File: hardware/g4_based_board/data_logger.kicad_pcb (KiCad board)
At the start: 4 copper layers, 100 x 100 mm, 115 parts, among them J1 Conn_01x07_Socket, J12 Screw_Terminal_01x04, J13 Conn_01x09_Pin, J2 Conn_02x07_Odd_Even, J3 Conn_01x07_Socket, J39 Conn_01x03, J4 Conn_01x04, J40 Conn_01x07_Socket, J43 Conn_01x06, J5 Screw_Terminal_01x03, J7 Conn_01x05_Socket, J8 USB_C_Receptacle_USB2.0, J9 Micro_SD_Card_Det1, Q1 NPN, Q2 NPN, Q5 NMOS, SW1 RESET, SW2 SW_SPDT, SW3 DOWN, SW7 UP, SW8 ENTER, SW9 WAKE, U1 STM32G431R6Tx, U2 MCP9804_MSOP, U3 MCP3428x-xST, U4 TL074, U6 tps2117, U7 AZ1117-3.3

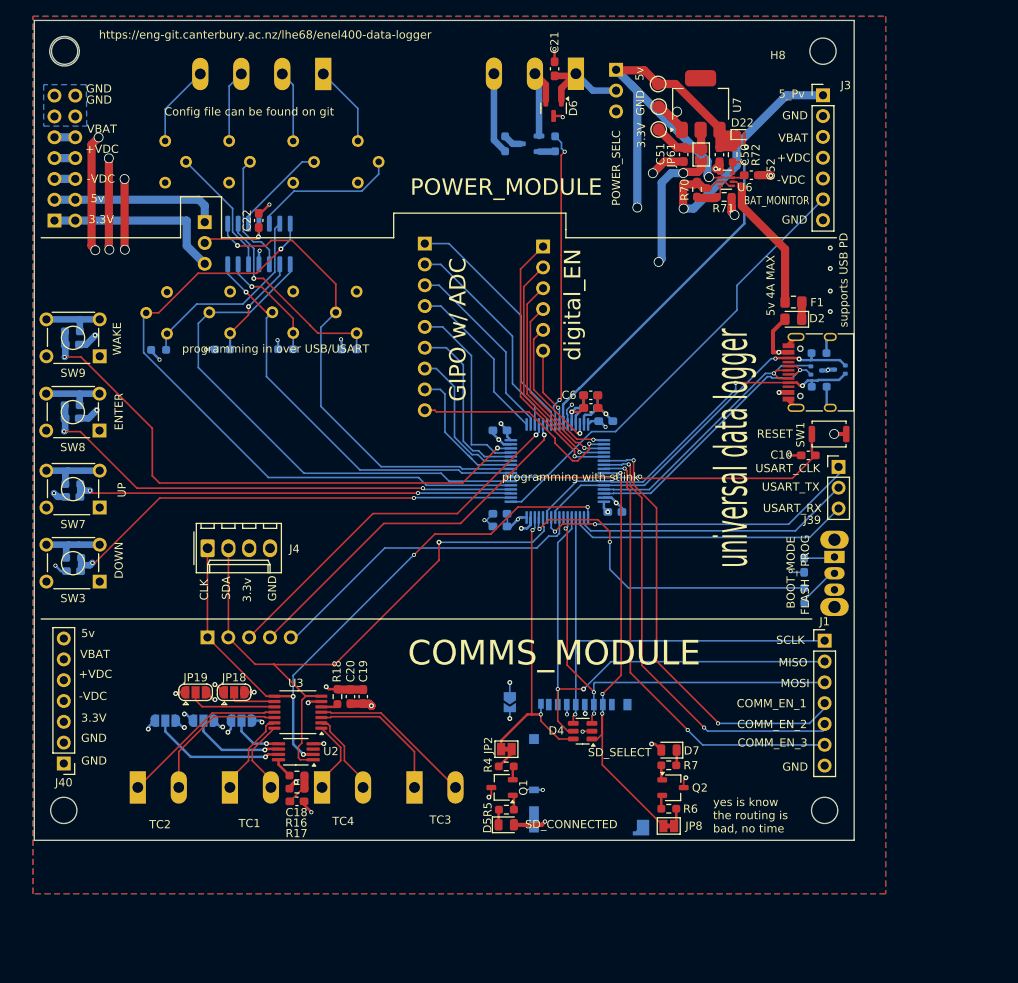
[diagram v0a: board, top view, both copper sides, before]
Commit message: minor addtion and swd header added and usart removed
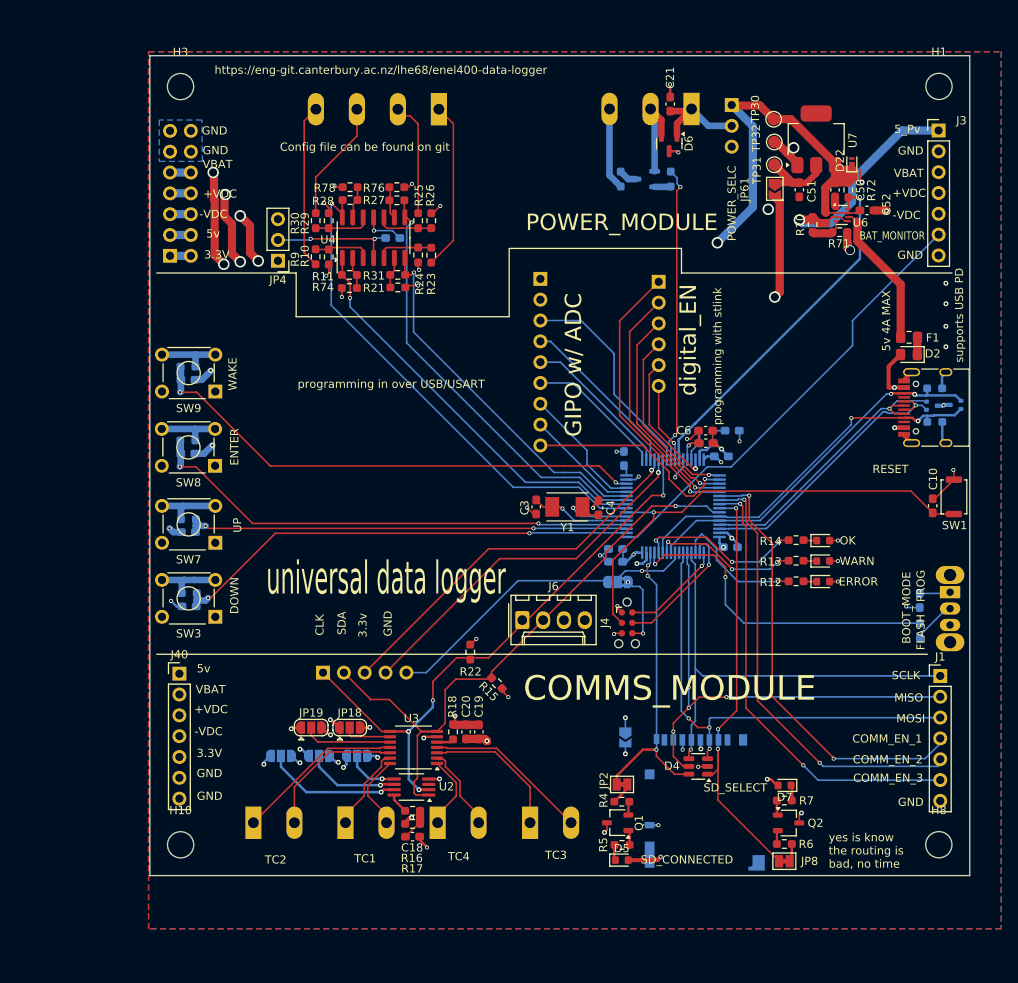
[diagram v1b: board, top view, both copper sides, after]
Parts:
- removed J39: Conn_01x03, Connector_PinHeader_2.54mm:PinHeader_1x03_P2.54mm_Vertical
- removed RV1, RV2, RV3, RV4, RV5, RV6, RV7, RV8: 10k, Potentiometer_THT:Potentiometer_Vishay_T73YP_Vertical
- added C3: 26p, Capacitor_SMD:C_0603_1608Metric_Pad1.08x0.95mm_HandSolder, F.Cu at (153.2, 103.0)
- added C4: 26p, Capacitor_SMD:C_0603_1608Metric_Pad1.08x0.95mm_HandSolder, F.Cu at (160.8, 103.1)
- added D10: LED, LED_SMD:LED_0603_1608Metric, F.Cu at (188.2, 112.1)
- added D8: LED, LED_SMD:LED_0603_1608Metric, F.Cu at (188.2, 107.1)
- added D9: LED, LED_SMD:LED_0603_1608Metric, F.Cu at (188.2, 109.6)
- added J6: Conn_01x04, Connector_Molex:Molex_KK-254_AE-6410-04A_1x04_P2.54mm_Vertical, F.Cu at (151.5, 116.8)
- added JP5: SWD_SPI, Jumper:SolderJumper-3_P1.3mm_Bridged2Bar12_RoundedPad1.0x1.5mm, B.Cu at (163.2, 112.2)
- added R10: 1k, Resistor_SMD:R_0603_1608Metric_Pad0.98x0.95mm_HandSolder, F.Cu at (127.9, 72.5)
- added R11: 1k, Resistor_SMD:R_0603_1608Metric_Pad0.98x0.95mm_HandSolder, F.Cu at (130.4, 74.7)
- added R12: R, Resistor_SMD:R_0603_1608Metric_Pad0.98x0.95mm_HandSolder, F.Cu at (184.9, 112.1)
- added R13: R, Resistor_SMD:R_0603_1608Metric_Pad0.98x0.95mm_HandSolder, F.Cu at (184.9, 109.6)
- added R14: R, Resistor_SMD:R_0603_1608Metric_Pad0.98x0.95mm_HandSolder, F.Cu at (184.9, 107.0)
- added R15: 4.7k, Resistor_SMD:R_0603_1608Metric_Pad0.98x0.95mm_HandSolder, F.Cu at (148.4, 124.5)
- added R22: 4.7k, Resistor_SMD:R_0603_1608Metric_Pad0.98x0.95mm_HandSolder, F.Cu at (145.2, 120.7)
- added R23: 1k, Resistor_SMD:R_0603_1608Metric_Pad0.98x0.95mm_HandSolder, F.Cu at (140.4, 72.3)
- added R24: 1k, Resistor_SMD:R_0603_1608Metric_Pad0.98x0.95mm_HandSolder, F.Cu at (138.8, 72.3)
- added R25: 1k, Resistor_SMD:R_0603_1608Metric_Pad0.98x0.95mm_HandSolder, F.Cu at (138.8, 68.1)
- added R26: 1k, Resistor_SMD:R_0603_1608Metric_Pad0.98x0.95mm_HandSolder, F.Cu at (140.4, 68.1)
- added R27: 1k, Resistor_SMD:R_0603_1608Metric_Pad0.98x0.95mm_HandSolder, F.Cu at (136.2, 65.6)
- added R28: 1k, Resistor_SMD:R_0603_1608Metric_Pad0.98x0.95mm_HandSolder, F.Cu at (130.5, 65.6)
- added R29: 1k, Resistor_SMD:R_0603_1608Metric_Pad0.98x0.95mm_HandSolder, F.Cu at (126.3, 68.1)
- added R30: 1k, Resistor_SMD:R_0603_1608Metric_Pad0.98x0.95mm_HandSolder, F.Cu at (127.9, 68.1)
- added R31: 1k, Resistor_SMD:R_0603_1608Metric_Pad0.98x0.95mm_HandSolder, F.Cu at (136.3, 74.7)
- added R8: 0, Resistor_SMD:R_0603_1608Metric, B.Cu at (173.9, 93.7)
- added R9: 1k, Resistor_SMD:R_0603_1608Metric_Pad0.98x0.95mm_HandSolder, F.Cu at (126.3, 72.5)
- added Y1: 8MHZ, 18PF, Crystal:Crystal_SMD_TXC_7A-2Pin_5x3.2mm, F.Cu at (157.0, 103.0)
- C22: moved to B.Cu
- D5, D7: footprint LED_SMD:LED_0805_2012Metric -> LED_SMD:LED_0603_1608Metric
- J4: value Conn_01x04 -> Conn_ARM_SWD_TagConnect_TC2030-NL; footprint Connector_Molex:Molex_KK-254_AE-6410-04A_1x04_P2.54mm_Vertical -> Connector:Tag-Connect_TC2030-IDC-NL_2x03_P1.27mm_Vertical
- JP4, R21, R74, R76, R78, U4: moved to F.Cu
- R19, R20: value R -> 1k
- moved H1 138.5 mm to (202.3, 51.7)
- moved H8 97.8 mm to (202.3, 144.2)
- moved H10 78.7 mm to (109.8, 144.2)
- moved J4 52.0 mm to (164.3, 117.1), turned to -90 degrees
- moved R21 30.2 mm to (136.3, 76.2), turned to 180 degrees
- moved R76 29.1 mm to (136.2, 64.0), turned to 180 degrees
- moved R78 21.3 mm to (130.5, 64.0)
- moved J40 17.9 mm to (109.7, 123.3), turned to 0 degrees
- moved C12 17.8 mm to (177.1, 93.7)
- moved SW1 17.0 mm to (204.2, 101.8), turned to -90 degrees
- moved C22 16.5 mm to (135.7, 70.2), turned to 0 degrees
- moved C10 16.4 mm to (201.6, 102.9), turned to -90 degrees
- moved C5 15.5 mm to (163.9, 97.1), turned to 90 degrees
- moved H3 14.8 mm to (109.8, 51.7)
- moved JP1 14.7 mm to (164.1, 131.1)
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- renumbered 5v to TP30, 3.3V to TP31, GND to TP32
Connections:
- C11 pad 1: +3.3V -> Net-(U1-VDDA)
- J12 pad 2: /analog_in/SIG_IN_2 -> /analog_in/SIG_IN_3
- J12 pad 3: /analog_in/SIG_IN_3 -> /analog_in/SIG_IN_4
- J12 pad 4: /analog_in/SIG_IN_4 -> /analog_in/SIG_IN_2
- J13 pad 1: /mcu/ADC-GPIO-PWM-12 -> GND
- J13 pad 2: /mcu/DAC2_OUT-ADC-GPIO-PWM -> +3.3V
- J13 pad 3: /mcu/DAC1_OUT-ADC-GPIO-PWM -> /mcu/ADC-GPIO-PWM-12
- J13 pad 4: /mcu/ADC-GPIO-PWM-4 -> /mcu/DAC2_OUT-ADC-GPIO-PWM
- J13 pad 5: /mcu/ADC-GPIO-PWM-2-DIFF1-2 -> /mcu/DAC1_OUT-ADC-GPIO-PWM
- J13 pad 6: /mcu/ADC-GPIO-PWM-1-DIFF1-1 -> /mcu/ADC-GPIO-PWM-4
- J13 pad 7: /mcu/ADC-GPIO-PWM-10 -> /mcu/ADC-GPIO-PWM-2-DIFF1-2
- J13 pad 8: /mcu/ADC-GPIO-PWM-9 -> /mcu/ADC-GPIO-PWM-1-DIFF1-1
- J4 pad 1: /high_speed_digital/I2C_CLK -> +3.3V
- J4 pad 2: /high_speed_digital/SDA -> /mcu/SWDIO
- J4 pad 3: +3.3V -> /mcu/NRST
- J4 pad 4: GND -> /mcu/SWD_CLK
- J40 pad 1: GND -> +5V
- J40 pad 2: GND -> +3.3V
- J40 pad 3: +3.3V -> +BATT
- J40 pad 4: -VDC -> +VDC
- J40 pad 5: +VDC -> -VDC
- J40 pad 6: +BATT -> GND
- J40 pad 7: +5V -> GND
- U1 pad 10: /mcu/ADC-GPIO-PWM-9 -> /analog_in/ADC_3
- U1 pad 11: /mcu/ADC-GPIO-PWM-10 -> /analog_in/ADC_1
- U1 pad 22: unconnected-(U1-PC4-Pad22) -> /high_speed_digital/I2C_CLK
- U1 pad 29: +3.3V -> Net-(U1-VDDA)
- U1 pad 42: unconnected-(U1-PA8-Pad42) -> /high_speed_digital/SDA
- U1 pad 49: /high_speed_digital/I2C_CLK -> /mcu/SWDIO
- U1 pad 50: /mcu/USART_TX -> /mcu/SWD_CLK
- U1 pad 51: /mcu/USART_RX -> /mcu/DEBUG_LED_1
- U1 pad 56: /high_speed_digital/SCLK -> /mcu/SP1_SCK_SWO
- U1 pad 58: /mcu/USART_CK -> /mcu/DEBUG_LED_2
- U1 pad 60: /high_speed_digital/SDA -> /mcu/DEBUG_LED_3
- U4 pad 7: /mcu/HSE_IN -> /analog_in/ADC_1
- U4 pad 8: /mcu/HSE_OUT -> /analog_in/ADC_3
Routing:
- net /mcu/HSE_IN: track 79.7 -> 12.1 mm
- net /mcu/HSE_OUT: track 64.0 -> 10.8 mm, vias 0 -> 1
- net /analog_in/ADC_3: track 0.00 -> 52.9 mm, vias 0 -> 1
- net /analog_in/ADC_1: track 0.00 -> 44.9 mm, vias 0 -> 1
- net /mcu/USART_CK: track 40.3 -> 0.00 mm, vias 2 -> 0
- net /mcu/USART_RX: track 34.5 -> 0.00 mm
- net /mcu/USART_TX: track 34.4 -> 0.00 mm
- net +5V: track 212.1 -> 181.5 mm, vias 2 -> 1
- net +3.3V: track 177.1 -> 148.8 mm, vias 17 -> 22
- net Net-(U4A--): track 24.8 -> 3.87 mm, vias 1 -> 0
- net Net-(U4B--): track 24.4 -> 3.81 mm
- net /mcu/DEBUG_LED_3: track 0.00 -> 20.5 mm, vias 0 -> 3
- net /mcu/ADC-GPIO-PWM-10: track 18.7 -> 0.00 mm
- net /mcu/DEBUG_LED_2: track 0.00 -> 17.9 mm, vias 0 -> 3
- net /mcu/ADC-GPIO-PWM-9: track 17.7 -> 0.00 mm
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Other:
- outline, holes or cut-outs redrawn
- board text added: "ERROR"
- board text added: "M3 hole size"
- board text added: "OK"
- board text added: "WARN"
- board text removed: "+dB"
- board text removed: "-dB"
- board text removed: "INPUT_GAIN"
- board text removed: "OUTPUT_GAIN"
- board text removed: "SIG_1"
- board text removed: "SIG_2"
- board text removed: "SIG_3"
- board text removed: "SIG_4"
- board text removed: "USART_CLK"
- board text removed: "USART_RX"
- board text removed: "USART_TX"

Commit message: auto updated
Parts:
- removed C53, C54, C55, C56: C, Capacitor_SMD:C_0603_1608Metric_Pad1.08x0.95mm_HandSolder
- removed D4: SP0505BAHT, Package_TO_SOT_SMD:SOT-23-6
- removed the G*** at (190.9, 133.5)
- removed the G*** at (169.9, 102.5)
- removed H10, H8: MountingHole, MountingHole:MountingHole_3.2mm_M3
- removed J13: Conn_01x09_Pin, Connector_PinHeader_2.54mm:PinHeader_1x09_P2.54mm_Vertical
- removed J43: Conn_01x06, Connector_PinHeader_2.54mm:PinHeader_1x06_P2.54mm_Vertical
- removed JP15, JP18, JP19: ~, Jumper:SolderJumper-3_P1.3mm_Open_RoundedPad1.0x1.5mm
- removed JP61: Jumper_2_Open, Jumper:SolderJumper-2_P1.3mm_Open_TrianglePad1.0x1.5mm
- removed R73, R75, R77, R79: R, Resistor_SMD:R_0603_1608Metric_Pad0.98x0.95mm_HandSolder
- removed SW3: DOWN, Button_Switch_THT:SW_TH_Tactile_Omron_B3F-10xx
- removed SW7: UP, Button_Switch_THT:SW_TH_Tactile_Omron_B3F-10xx
- removed SW8: ENTER, Button_Switch_THT:SW_TH_Tactile_Omron_B3F-10xx
- removed SW9: WAKE, Button_Switch_THT:SW_TH_Tactile_Omron_B3F-10xx
- added C14: 1u, Capacitor_SMD:C_0603_1608Metric_Pad1.08x0.95mm_HandSolder, F.Cu at (110.5, 81.2)
- added C15: 0.1u, Capacitor_SMD:C_0603_1608Metric_Pad1.08x0.95mm_HandSolder, B.Cu at (121.0, 149.4)
- added C16: 0.1u, Capacitor_SMD:C_0603_1608Metric_Pad1.08x0.95mm_HandSolder, B.Cu at (121.0, 145.4)
- added C17: 10u, Capacitor_SMD:C_0603_1608Metric_Pad1.08x0.95mm_HandSolder, B.Cu at (121.0, 143.9)
- added C23: 1u, Capacitor_SMD:C_0603_1608Metric_Pad1.08x0.95mm_HandSolder, F.Cu at (105.7, 81.2)
- added C24: 1u, Capacitor_SMD:C_0603_1608Metric_Pad1.08x0.95mm_HandSolder, F.Cu at (110.4, 70.5)
- added C25: 1u, Capacitor_SMD:C_0603_1608Metric_Pad1.08x0.95mm_HandSolder, F.Cu at (112.0, 70.5)
- added C26: 1u, Capacitor_SMD:C_0603_1608Metric_Pad1.08x0.95mm_HandSolder, F.Cu at (107.3, 70.5)
- added C27: 1u, Capacitor_SMD:C_0603_1608Metric_Pad1.08x0.95mm_HandSolder, F.Cu at (108.8, 70.5)
- added C28: 100n, Capacitor_SMD:C_0603_1608Metric_Pad1.08x0.95mm_HandSolder, F.Cu at (154.9, 153.6)
- added C29: 100n, Capacitor_SMD:C_0603_1608Metric_Pad1.08x0.95mm_HandSolder, F.Cu at (158.6, 129.2)
- added C30: 100n, Capacitor_SMD:C_0603_1608Metric_Pad1.08x0.95mm_HandSolder, F.Cu at (162.0, 129.2)
- added C31: 100n, Capacitor_SMD:C_0603_1608Metric_Pad1.08x0.95mm_HandSolder, F.Cu at (173.6, 122.5)
- added C32: 100n, Capacitor_SMD:C_0603_1608Metric_Pad1.08x0.95mm_HandSolder, F.Cu at (177.1, 122.5)
- added C33: 10u, Capacitor_SMD:C_0603_1608Metric_Pad1.08x0.95mm_HandSolder, F.Cu at (97.4, 81.7)
- added D12: SP0502BAHT, Package_TO_SOT_SMD:SOT-23, B.Cu at (137.6, 69.7)
- added D13: LED, LED_SMD:LED_0603_1608Metric, F.Cu at (101.1, 64.8)
- added D14: LED, LED_SMD:LED_0603_1608Metric, F.Cu at (102.8, 64.8)
- added D15: LED, LED_SMD:LED_0603_1608Metric, F.Cu at (101.3, 88.0)
- added G***: LOGO, frogs:frog_smaller, F.Cu at (124.7, 103.6)
- added H2: MountingHole_Pad, MountingHole:MountingHole_3.2mm_M3_DIN965_Pad_TopOnly, F.Cu at (186.5, 62.5)
- added H4: MountingHole_Pad, MountingHole:MountingHole_3.2mm_M3_DIN965_Pad_TopOnly, F.Cu at (186.5, 155.5)
- added J11: Conn_01x06_Pin, Connector_JST:JST_XH_B6B-XH-A_1x06_P2.50mm_Vertical, F.Cu at (186.7, 90.0)
- added J15: Screw_Terminal_01x03, TerminalBlock:TerminalBlock_Altech_AK300-3_P5.00mm, F.Cu at (134.7, 65.5)
- added J16: Conn_01x09, Connector_JST:JST_XH_B9B-XH-A_1x09_P2.50mm_Vertical, F.Cu at (185.6, 129.0)
- added JP10: ~, Jumper:SolderJumper-3_P1.3mm_Open_RoundedPad1.0x1.5mm, B.Cu at (128.0, 157.4)
- added JP11: ~, Jumper:SolderJumper-3_P1.3mm_Open_RoundedPad1.0x1.5mm, B.Cu at (131.3, 144.6)
- added JP12: ~, Jumper:SolderJumper-3_P1.3mm_Open_RoundedPad1.0x1.5mm, B.Cu at (131.3, 142.0)
- added JP6: power_select, Connector_PinHeader_2.54mm:PinHeader_1x03_P2.54mm_Vertical, F.Cu at (150.2, 63.9)
- added JP7: ~, Jumper:SolderJumper-3_P1.3mm_Open_RoundedPad1.0x1.5mm, B.Cu at (120.8, 157.3)
- added JP9: ~, Jumper:SolderJumper-3_P1.3mm_Open_RoundedPad1.0x1.5mm, B.Cu at (124.4, 156.3)
- added Q3: PMOS, Package_TO_SOT_SMD:SOT-23-3, F.Cu at (180.6, 131.2)
- added Q4: PMOS, Package_TO_SOT_SMD:SOT-23-3, F.Cu at (180.5, 103.1)
- added Q6: PMOS, Package_TO_SOT_THT:TO-247-3_Vertical, B.Cu at (134.6, 75.0)
- added Q7: 2N3904, Package_TO_SOT_THT:TO-92_Inline, F.Cu at (127.2, 81.3)
- added Q8: 2N3904, Package_TO_SOT_THT:TO-92_Inline, F.Cu at (136.8, 82.2)
- added R32: 4.7k, Resistor_SMD:R_0603_1608Metric_Pad0.98x0.95mm_HandSolder, F.Cu at (149.4, 148.3)
- added R33: 10, Resistor_SMD:R_0603_1608Metric_Pad0.98x0.95mm_HandSolder, F.Cu at (139.2, 78.5)
- added R34: 10, Resistor_SMD:R_0603_1608Metric_Pad0.98x0.95mm_HandSolder, F.Cu at (177.6, 103.1)
- added R35: R, Resistor_SMD:R_0603_1608Metric_Pad0.98x0.95mm_HandSolder, F.Cu at (101.1, 68.0)
- added R36: R, Resistor_SMD:R_0603_1608Metric_Pad0.98x0.95mm_HandSolder, F.Cu at (102.8, 68.0)
- added R37: 10, Resistor_SMD:R_0603_1608Metric_Pad0.98x0.95mm_HandSolder, F.Cu at (177.7, 131.2)
- added R38: 4.7k, Resistor_SMD:R_0603_1608Metric_Pad0.98x0.95mm_HandSolder, F.Cu at (180.0, 123.4)
- added R39: 4.7k, Resistor_SMD:R_0603_1608Metric_Pad0.98x0.95mm_HandSolder, F.Cu at (180.0, 126.8)
- added R40: R, Resistor_SMD:R_0603_1608Metric_Pad0.98x0.95mm_HandSolder, F.Cu at (101.3, 84.8)
- added R41: 4.7k, Resistor_SMD:R_0603_1608Metric_Pad0.98x0.95mm_HandSolder, F.Cu at (136.6, 100.2)
- added R42: 4.7k, Resistor_SMD:R_0603_1608Metric_Pad0.98x0.95mm_HandSolder, F.Cu at (136.6, 103.6)
- added R43: 0, Resistor_SMD:R_0603_1608Metric_Pad0.98x0.95mm_HandSolder, F.Cu at (180.9, 97.3)
- added R44: 0, Resistor_SMD:R_0603_1608Metric_Pad0.98x0.95mm_HandSolder, F.Cu at (180.9, 94.9)
- added R45: 0, Resistor_SMD:R_0603_1608Metric_Pad0.98x0.95mm_HandSolder, F.Cu at (180.9, 100.0)
- added R46: R, Resistor_SMD:R_0603_1608Metric_Pad0.98x0.95mm_HandSolder, F.Cu at (92.0, 85.2)
- added R47: 1k, Resistor_SMD:R_0603_1608Metric_Pad0.98x0.95mm_HandSolder, F.Cu at (178.8, 133.7)
- added R48: 1k, Resistor_SMD:R_0603_1608Metric_Pad0.98x0.95mm_HandSolder, F.Cu at (178.6, 105.6)
- added R49: 10k, Resistor_SMD:R_0603_1608Metric_Pad0.98x0.95mm_HandSolder, F.Cu at (121.4, 78.5)
- added R50: 10k, Resistor_SMD:R_0603_1608Metric_Pad0.98x0.95mm_HandSolder, F.Cu at (135.6, 78.5)
- added R51: 10k, Resistor_SMD:R_0603_1608Metric_Pad0.98x0.95mm_HandSolder, F.Cu at (134.4, 82.2)
- added R52: 10k, Resistor_SMD:R_0603_1608Metric_Pad0.98x0.95mm_HandSolder, F.Cu at (129.5, 82.2)
- added R53: 4.7k, Resistor_SMD:R_0603_1608Metric_Pad0.98x0.95mm_HandSolder, F.Cu at (181.5, 90.0)
- added TP1: TestPoint, TestPoint:TestPoint_Keystone_5015_Micro-Minature, F.Cu at (138.6, 136.2)
- added TP2: TestPoint, TestPoint:TestPoint_Keystone_5015_Micro-Minature, F.Cu at (138.6, 138.9)
- added TP4: TestPoint, TestPoint:TestPoint_Pad_2.0x2.0mm, F.Cu at (122.8, 88.9)
- added TP5: TestPoint, TestPoint:TestPoint_Pad_2.0x2.0mm, F.Cu at (119.7, 88.9)
- added TP6: TestPoint, TestPoint:TestPoint_Pad_2.0x2.0mm, F.Cu at (116.5, 88.9)
- added U10: TCA9800, Package_SO:VSSOP-8_3.0x3.0mm_P0.65mm, F.Cu at (160.2, 126.7)
- added U11: TCA9800, Package_SO:VSSOP-8_3.0x3.0mm_P0.65mm, F.Cu at (175.5, 125.2)
- added U5: CM1624, Package_DFN_QFN:OnSemi_UDFN-16-1EP_1.35x3.3mm_P0.4mm_EP0.4x2.8mm, F.Cu at (110.0, 121.8)
- added U8: BME680, Package_LGA:Bosch_LGA-8_3x3mm_P0.8mm_ClockwisePinNumbering, F.Cu at (152.6, 150.9)
- C10, C2, C3, C4, C6, D6, JP2, JP8, Q1, Q2, R16, R17, R18, R4, R5, R6, R7, U2, Y1: moved to B.Cu
- C18: value 0.1u -> 100n
- C19: value 0.1u -> 10u
- C20: value 10u -> 1u
- C21: value C -> 1u
- H1, H3: value MountingHole -> MountingHole_Pad; footprint MountingHole:MountingHole_3.2mm_M3 -> MountingHole:MountingHole_3.2mm_M3_DIN965_Pad_TopOnly
- J12, J5, J9, SW2, TC1, TC2, TC3, TC4, U1: moved to F.Cu
- J2: value Conn_02x07_Odd_Even -> Conn_01x07_Socket; footprint Connector_PinHeader_2.54mm:PinHeader_2x07_P2.54mm_Vertical -> Connector_PinHeader_2.54mm:PinHeader_1x07_P2.54mm_Vertical; moved to F.Cu
- J4: footprint Connector:Tag-Connect_TC2030-IDC-NL_2x03_P1.27mm_Vertical -> Connector:Tag-Connect_TC2030-IDC-FP_2x03_P1.27mm_Vertical
- J6: footprint Connector_Molex:Molex_KK-254_AE-6410-04A_1x04_P2.54mm_Vertical -> Connector_PinHeader_2.54mm:PinHeader_1x04_P2.54mm_Vertical; moved to B.Cu
- J7: value Conn_01x05_Socket -> Conn_01x10; footprint Connector_PinHeader_2.54mm:PinHeader_1x05_P2.54mm_Vertical -> Connector_PinHeader_2.54mm:PinHeader_1x10_P2.54mm_Vertical
- JP16, JP17: value ~ -> Jumper_2_Open; footprint Jumper:SolderJumper-3_P1.3mm_Open_RoundedPad1.0x1.5mm -> Jumper:SolderJumper-2_P1.3mm_Open_TrianglePad1.0x1.5mm; moved to F.Cu
- JP3: value power_select -> ~; footprint Connector_PinHeader_2.54mm:PinHeader_1x03_P2.54mm_Vertical -> Jumper:SolderJumper-3_P1.3mm_Open_RoundedPad1.0x1.5mm; moved to F.Cu
- Q5: value NMOS -> PMOS; footprint Package_TO_SOT_SMD:SOT-23-3 -> Package_TO_SOT_THT:TO-247-3_Vertical
- R19: value 1k -> 10; moved to F.Cu
- R20: value 1k -> 4.7k; moved to F.Cu
- R70: value 10k -> 16.9k
- R71: value 10k -> 5k
- moved D1 112.2 mm to (92.2, 92.2), turned to 0 degrees
- moved SW2 111.5 mm to (92.4, 106.9)
- moved SW1 111.1 mm to (93.1, 100.9), turned to 0 degrees
- moved J1 109.5 mm to (93.5, 134.6)
- moved J3 109.4 mm to (93.4, 67.4)
- moved H1 109.4 mm to (93.5, 62.5)
- moved C10 108.5 mm to (93.1, 100.8), turned to 0 degrees
- moved J8 108.2 mm to (94.0, 92.0), turned to -90 degrees
- moved R2 107.7 mm to (94.3, 94.8), turned to 180 degrees
- moved R3 107.7 mm to (94.2, 89.2), turned to 180 degrees
- moved D3 106.7 mm to (94.7, 92.2)
- moved H3 105.0 mm to (93.5, 155.5)
- moved R1 104.3 mm to (96.1, 109.0), turned to -90 degrees
- moved D2 101.2 mm to (97.5, 85.6), turned to 0 degrees
- moved F1 101.2 mm to (97.5, 83.6), turned to 180 degrees
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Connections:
- net /high_speed_digital/thermocouples/T1_+ renamed /high_speed_digital/T1_+
- net /high_speed_digital/thermocouples/T1_- renamed /high_speed_digital/T1_-
- net /high_speed_digital/thermocouples/T2_+ renamed /high_speed_digital/T2_+
- net /high_speed_digital/thermocouples/T2_- renamed /high_speed_digital/T2_-
- net /high_speed_digital/thermocouples/T3_+ renamed /high_speed_digital/T3_+
- net /high_speed_digital/thermocouples/T3_- renamed /high_speed_digital/T3_-
- net /high_speed_digital/thermocouples/T4_+ renamed /high_speed_digital/T4_+
- net /high_speed_digital/thermocouples/T4_- renamed /high_speed_digital/T4_-
- C1 pad 1: +3.3V -> /V_bat_monitor
- C18 pad 1: Net-(C18-Pad1) -> +3.3V
- C19 pad 1: +3.3V -> /power_amp/PWR
- C20 pad 1: +3.3V -> +5V
- C21 pad 1: Net-(J5-Pin_1) -> +5V
- C51 pad 1: Net-(JP61-A) -> +3.3V
- D6 pad 1: Net-(J5-Pin_1) -> /power_amp/PWR
- J2 pad 1: +3.3V -> GND
- J2 pad 2: +3.3V -> GND
- J2 pad 3: +5V -> +3.3V
- J2 pad 4: +5V -> -VDC
- J2 pad 5: -VDC -> +VDC
- J2 pad 6: -VDC -> +BATT
- J2 pad 7: +VDC -> +5V
- J40 pad 1: +5V -> GND
- J40 pad 2: +3.3V -> GND
- J40 pad 3: +BATT -> +3.3V
- J40 pad 4: +VDC -> +BATT
- J40 pad 5: -VDC -> +VDC
- J40 pad 6: GND -> -VDC
- J40 pad 7: GND -> +5V
- J5 pad 1: Net-(J5-Pin_1) -> /power_amp/PWR
- J6 pad 1: /high_speed_digital/I2C_CLK -> +3.3V
- J6 pad 2: /high_speed_digital/SDA -> Net-(J6-Pin_2)
- J6 pad 3: +3.3V -> Net-(J6-Pin_3)
- J7 pad 1: /high_speed_digital/I2C_CLK -> GND
- J7 pad 2: /high_speed_digital/SDA -> +3.3V
- J7 pad 3: /high_speed_digital/MISO -> /mcu/ADC-GPIO-PWM-7
- J7 pad 4: /high_speed_digital/MOSI -> /mcu/ADC-GPIO-PWM-8
- J7 pad 5: /high_speed_digital/SCLK -> /mcu/ADC-GPIO-PWM-9
- J8 pad S1: GND -> GNDS
- J9 pad 3: /interface/MOSI -> /interface/MOSI_SD
- J9 pad 7: /interface/MISO -> /interface/MISO_SD
- JP16 pad 1: GND -> Net-(JP16-A)
- JP16 pad 2: Net-(JP16-C) -> GND
- JP17 pad 1: GND -> Net-(JP17-A)
- JP17 pad 2: Net-(JP17-C) -> GND
- JP3 pad 1: +5V -> +3.3V
- JP3 pad 2: Net-(J5-Pin_1) -> Net-(JP3-C)
- JP3 pad 3: +BATT -> GND
- Q5 pad 1: Net-(J5-Pin_2) -> /power_amp/PWR
- Q5 pad 3: Net-(Q5-S) -> Net-(J5-Pin_2)
- R15 pad 2: /high_speed_digital/SDA -> Net-(J6-Pin_3)
- R16 pad 1: +3.3V -> Net-(R16-Pad1)
- R16 pad 2: Net-(C18-Pad1) -> Net-(U2-V_{DD})
- R17 pad 1: Net-(C18-Pad1) -> +3.3V
- R17 pad 2: Net-(U2-V_{DD}) -> Net-(R16-Pad1)
- R19 pad 2: /mcu/ADC-GPIO-PWM-11 -> Net-(Q7-C)
- R20 pad 1: Net-(Q5-S) -> +3.3V
- R20 pad 2: GND -> /high_speed_digital/SDA
- R22 pad 2: /high_speed_digital/I2C_CLK -> Net-(J6-Pin_2)
- R23 pad 2: /analog_in/SIG_IN_1 -> /analog_in/SIG_IN_4
- R29 pad 2: /analog_in/SIG_IN_4 -> /analog_in/SIG_IN_1
- TP31 pad 1: Net-(JP61-A) -> +3.3V
- U1 pad 10: /analog_in/ADC_3 -> /mcu/ADC-GPIO-PWM-9
- U1 pad 11: /analog_in/ADC_1 -> /mcu/ADC-GPIO-PWM-10
- U1 pad 13: /mcu/ADC-GPIO-PWM-2-DIFF1-2 -> /analog_in/ADC_2
- U1 pad 14: /interface/WAKE_BTN -> /high_speed_digital/BTN_1
- U1 pad 17: /mcu/ADC-GPIO-PWM-4 -> /analog_in/ADC_1
- U1 pad 2: /interface/DOWN_BTN -> /mcu/COMMS_EN_1
- U1 pad 23: /mcu/ADC-GPIO-PWM-12 -> /analog_in/ADC_3
- U1 pad 24: /mcu/ADC-GPIO-PWM-11 -> /analog_in/ADC_4
- U1 pad 25: /mcu/DIGITAL_IO_EN_4 -> /mcu/PWM_2
- U1 pad 26: /mcu/PWR_STATUS -> /mcu/PWM_1
- U1 pad 3: /interface/UP_BTN -> /mcu/COMMS_EN_2
- U1 pad 33: /mcu/DIGITAL_IO_EN_6 -> /high_speed_digital/CS
- U1 pad 35: /mcu/DIGITAL_IO_EN_1 -> /high_speed_digital/CAMERA_POWER_EN
- U1 pad 36: /mcu/DIGITAL_IO_EN_2 -> /high_speed_digital/HI_POWER_EN
- U1 pad 38: /mcu/COMMS_EN_1 -> /high_speed_digital/BTN_4
- U1 pad 39: /mcu/COMMS_EN_2 -> /high_speed_digital/BTN_2
- U1 pad 4: /interface/ENTER_BTN -> /mcu/COMMS_EN_3
- U1 pad 40: /mcu/COMMS_EN_3 -> /high_speed_digital/BTN_3
- U1 pad 41: /interface/SD_SELECT -> /mcu/PWR_STATUS
- U1 pad 51: /mcu/DEBUG_LED_1 -> /interface/SD_CARD_SELECT
- U1 pad 55: unconnected-(U1-PD2-Pad55) -> /mcu/DEBUG_LED_1
- U1 pad 8: /analog_in/ADC_4 -> /mcu/ADC-GPIO-PWM-7
- U1 pad 9: /analog_in/ADC_2 -> /mcu/ADC-GPIO-PWM-8
- U2 pad 1: /high_speed_digital/SDA -> /high_speed_digital/I2C_CLK
- U2 pad 2: /high_speed_digital/I2C_CLK -> /high_speed_digital/SDA
- U2 pad 5: Net-(JP17-C) -> Net-(JP10-C)
- U2 pad 6: Net-(JP16-C) -> Net-(JP9-C)
- U3 pad 7: /high_speed_digital/SDA -> /high_speed_digital/I2C_CLK
- U3 pad 8: /high_speed_digital/I2C_CLK -> /high_speed_digital/SDA
- U7 pad 2: Net-(JP61-A) -> +3.3V
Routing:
- net /high_speed_digital/BTN_3: track 0.00 -> 77.3 mm, vias 0 -> 6
- net /power_amp/PWR: track 0.00 -> 76.9 mm
- net /high_speed_digital/BTN_2: track 0.00 -> 76.3 mm, vias 0 -> 6
- net /high_speed_digital/HI_POWER_EN: track 0.00 -> 75.9 mm, vias 0 -> 6
- net /high_speed_digital/BTN_4: track 0.00 -> 74.8 mm, vias 0 -> 6
- net /high_speed_digital/I2C_CLK: track 71.8 -> 146.0 mm, vias 4 -> 1
- net /high_speed_digital/SDA: track 75.6 -> 146.6 mm, vias 1 -> 4
- net /high_speed_digital/CS: track 0.00 -> 68.4 mm, vias 0 -> 2
- net /interface/WAKE_BTN: track 62.3 -> 0.00 mm, vias 2 -> 0
- net /interface/ENTER_BTN: track 60.6 -> 0.00 mm, vias 2 -> 0
- net /high_speed_digital/BTN_1: track 0.00 -> 58.8 mm, vias 0 -> 2
- net /high_speed_digital/CAMERA_POWER_EN: track 0.00 -> 57.9 mm, vias 0 -> 4
- net /interface/DOWN_BTN: track 57.5 -> 0.00 mm, vias 2 -> 0
- net +5V: track 181.5 -> 236.6 mm, vias 1 -> 3
- net /interface/UP_BTN: track 54.3 -> 0.00 mm, vias 2 -> 0
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- added copper zone on F.Cu, net +3.3V
- added copper zone on In2.Cu, net +3.3V
- added copper zone on F.Cu, net +5V
- added copper zone on In1.Cu, net GND
- added copper zone on F.Cu, net GNDS
- removed copper zone on In1.Cu, net +3.3V
- removed copper zone on B.Cu, net GND
- removed copper zone on F.Cu, net GND
- removed copper zone on In2.Cu, net GND
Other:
- outline, holes or cut-outs redrawn
- board text added: "3v3"
- board text added: "5v_IN"
- board text added: "6-pin plug-o-nails"
- board text added: "ADC3"
- board text added: "ADC_1"
- board text added: "ADC_10"
- board text added: "ADC_1_DAC_1"
- board text added: "ADC_1_DAC_2"
- board text added: "ADC_7"
- board text added: "ADC_8"
- board text added: "ADC_9"
- board text added: "BAT"
- board text added: "BTN1"
- board text added: "BTN2"
- board text added: "BTN3"
- board text added: "BTN4"
- board text added: "CONN"
- board text added: "CS"
- board text added: "DATALOGGER"
- board text added: "DEVICE_INFO"
- board text added: "GO TOUCH GRASS"
- board text added: "I2C_PULL_UP"
- board text added: "IO1"
- board text added: "IO2"
- board text added: "IO3"
- board text added: "IO5"
- board text added: "PROG--FLASH"
- board text added: "PWR STATUS"
- board text added: "SLEC"
- board text added: "STM32_G4"
- board text added: "V_MONITOR"
- board text removed: "3.3V"
- board text removed: "5_Pv"
- board text removed: "5v 4A MAX"
- board text removed: "ADC-10"
- board text removed: "ADC-12"
- board text removed: "ADC-1_DIFF_1"
- board text removed: "ADC-2_DIFF_2"
- board text removed: "ADC-3"
- board text removed: "ADC-4"
- board text removed: "ADC-9"
- board text removed: "BAT_MONITOR"
- board text removed: "BOOT_MODE"
- board text removed: "COMM_EN_1"
- board text removed: "COMM_EN_2"
- board text removed: "COMM_EN_3"
- board text removed: "Config file can be found on git"
- board text removed: "DAC1"
- board text removed: "DAC2"
- board text removed: "DOWN"
- board text removed: "EN-1"
- board text removed: "EN-2"
- board text removed: "EN-3"
- board text removed: "EN-4"
- board text removed: "EN-5"
- board text removed: "EN-6"
- board text removed: "ENEL-400W-GROUP-E31"
- board text removed: "ENTER"
- board text removed: "FLASH"
- board text removed: "GIPO w/ ADC"
- board text removed: "ID: 72740637"
- board text removed: "LOGAN HENDERSON"
- board text removed: "M3 hole size"
- board text removed: "POWER_SELC"
- board text removed: "PROG"
- board text removed: "PWM-GND"
- board text removed: "PWR"
- board text removed: "SD CARD"
- board text removed: "SD_CONNECTED"
- board text removed: "SD_SELECT"
- board text removed: "SIG_1_IN"
- board text removed: "SIG_2_IN"
- board text removed: "SIG_3_IN"
- board text removed: "SIG_4_IN"
- board text removed: "STM32G431RBT6"
- board text removed: "TC1"
- board text removed: "TC2"
- board text removed: "TC3"
- board text removed: "TC4"
- board text removed: "UP"
- board text removed: "WAKE"
- board text removed: "digital_EN"
- board text removed: "programming in over USB/USART"
- board text removed: "programming with stlink"
- board text removed: "supports USB PD"
- board text removed: "universal data logger"
- board text removed: "yes is know the routing is bad, no time"
